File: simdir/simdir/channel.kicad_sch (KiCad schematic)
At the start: 80 parts, among them Q1 BC847, Q10 BC847, Q11 BC847, Q12 BC847, Q13 BC847, Q14 BC847, Q15 BC847, Q16 BC847, Q2 BC847, Q3 BC847, Q4 BC847, Q5 BC847, Q6 BC847, Q7 BC847, Q8 BC847, Q9 BC847, U1 MASWSS0178, U10 MASWSS0178, U11 MASWSS0178, U12 MASWSS0178, U13 MASWSS0178, U14 MASWSS0178, U15 MASWSS0178, U16 MASWSS0178, U17 LTV-847S, U18 LTV-847S, U19 74HCT595, U2 MASWSS0178, U3 MASWSS0178, U4 MASWSS0178, U5 MASWSS0178, U6 MASWSS0178, U7 MASWSS0178, U8 MASWSS0178, U9 MASWSS0178

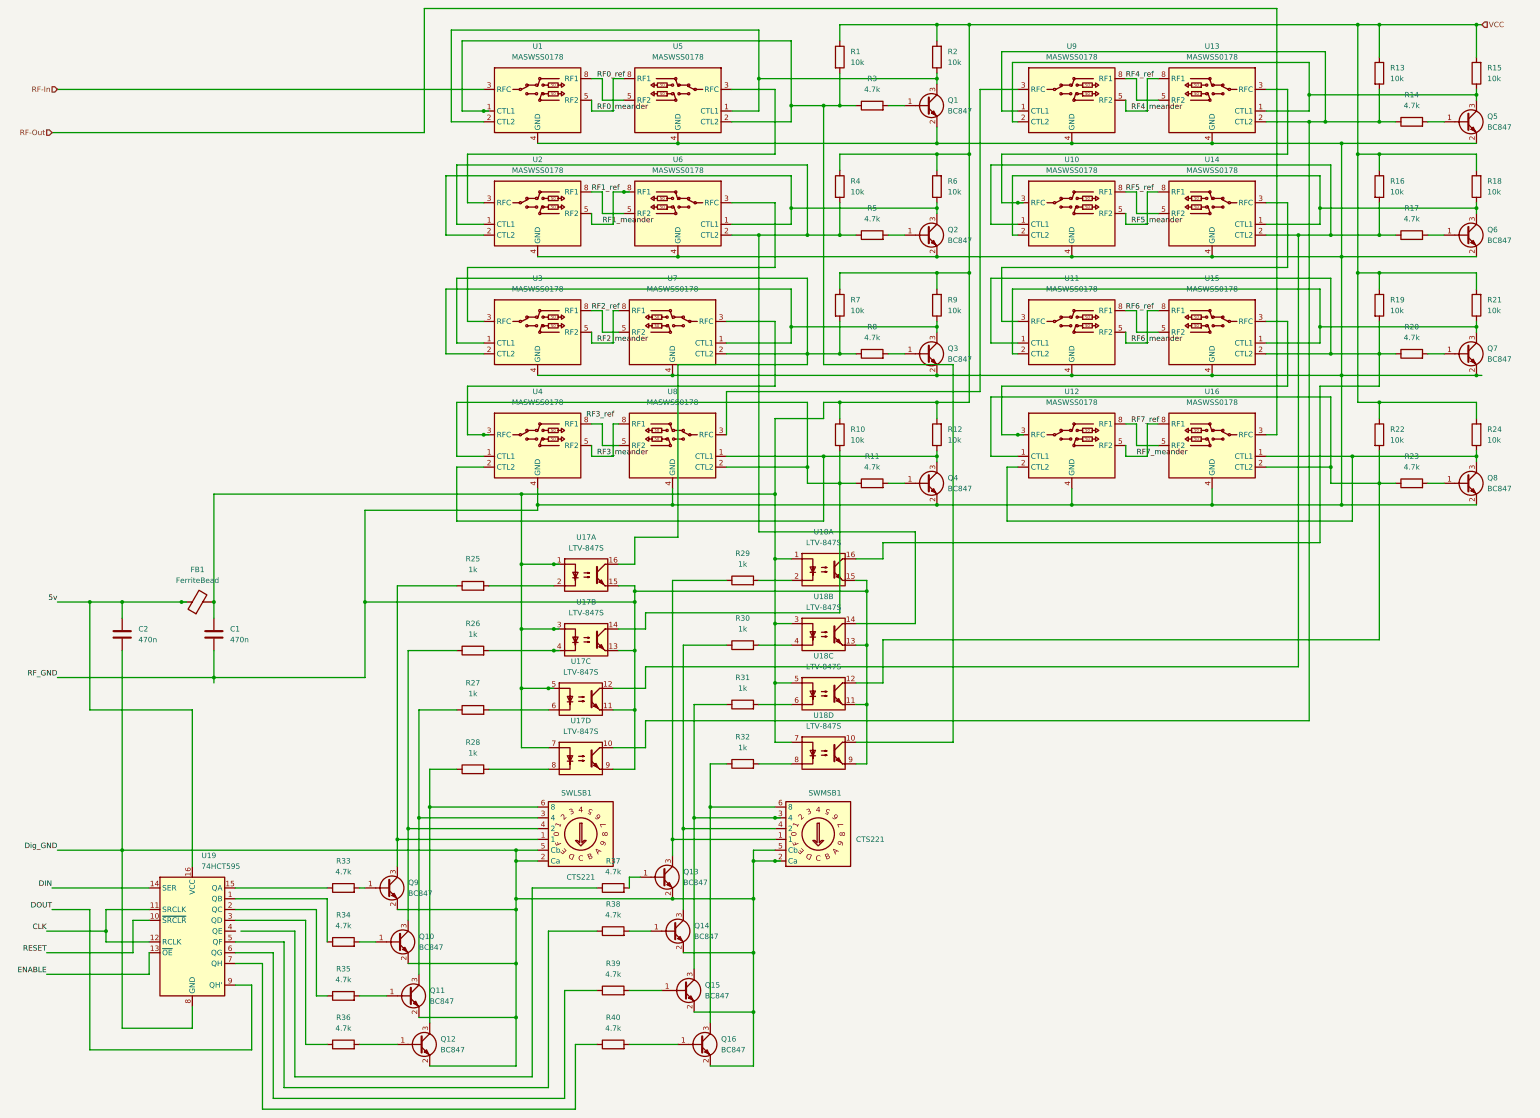
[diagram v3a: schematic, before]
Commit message: Finished channel layout.
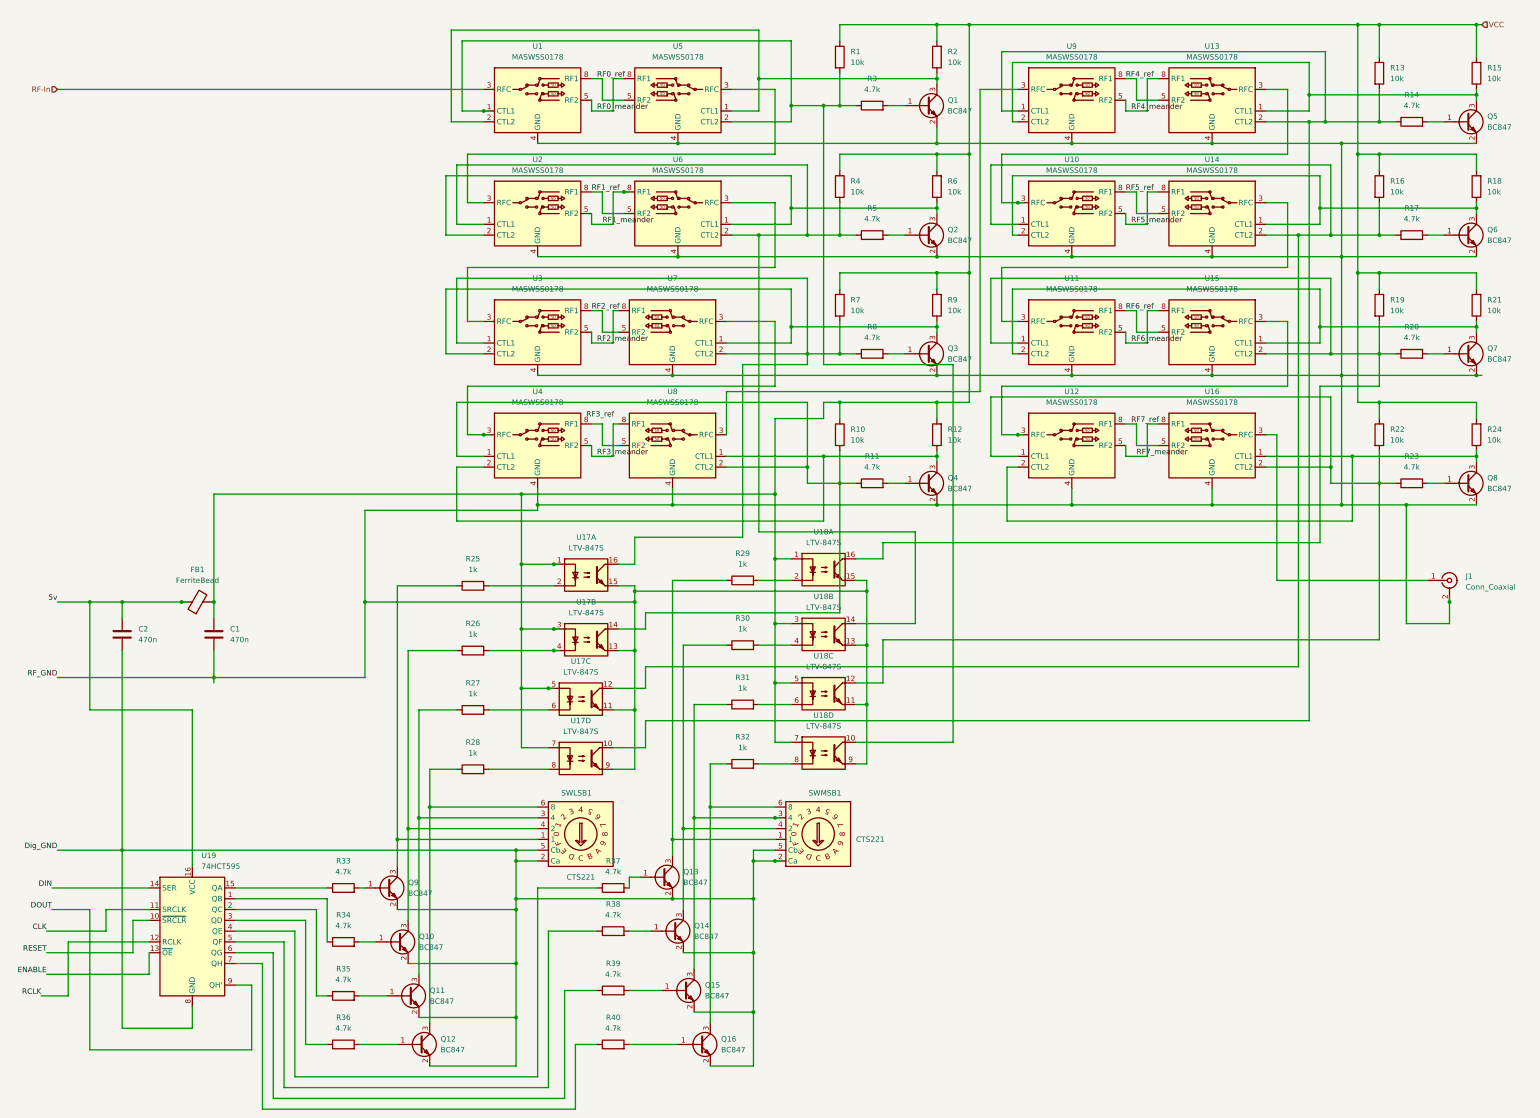
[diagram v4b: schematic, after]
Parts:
- added J1: Conn_Coaxial, Connector_Coaxial:SMA_Amphenol_132289_EdgeMount, symbol Connector:Conn_Coaxial
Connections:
- net CLK: no longer U19.12 (RCLK)
- net RF_GND: now also J1.2 (Ext)
- net at U19.4 (QE): now also R37.1
- net RF-Out: no longer names the net of U16.3 (RFC)
- net RF-Out: now also J1.1 (In)
- new net RCLK: U19.12 (RCLK)

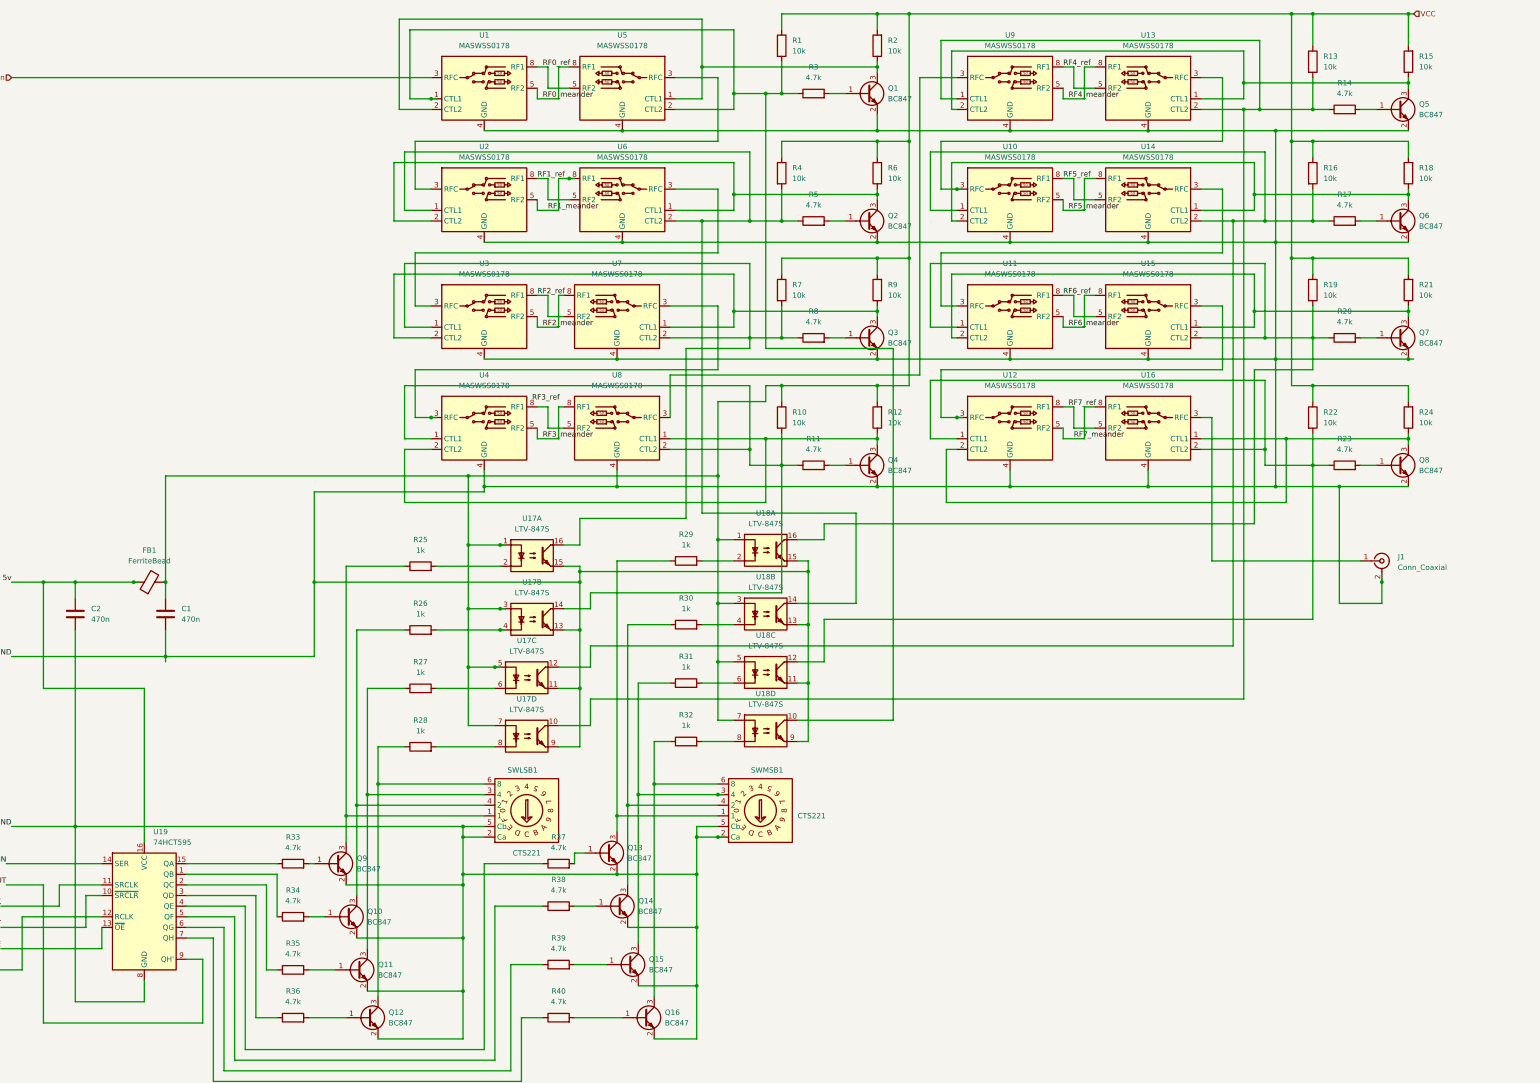
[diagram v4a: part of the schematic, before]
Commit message: Finalized channel design.
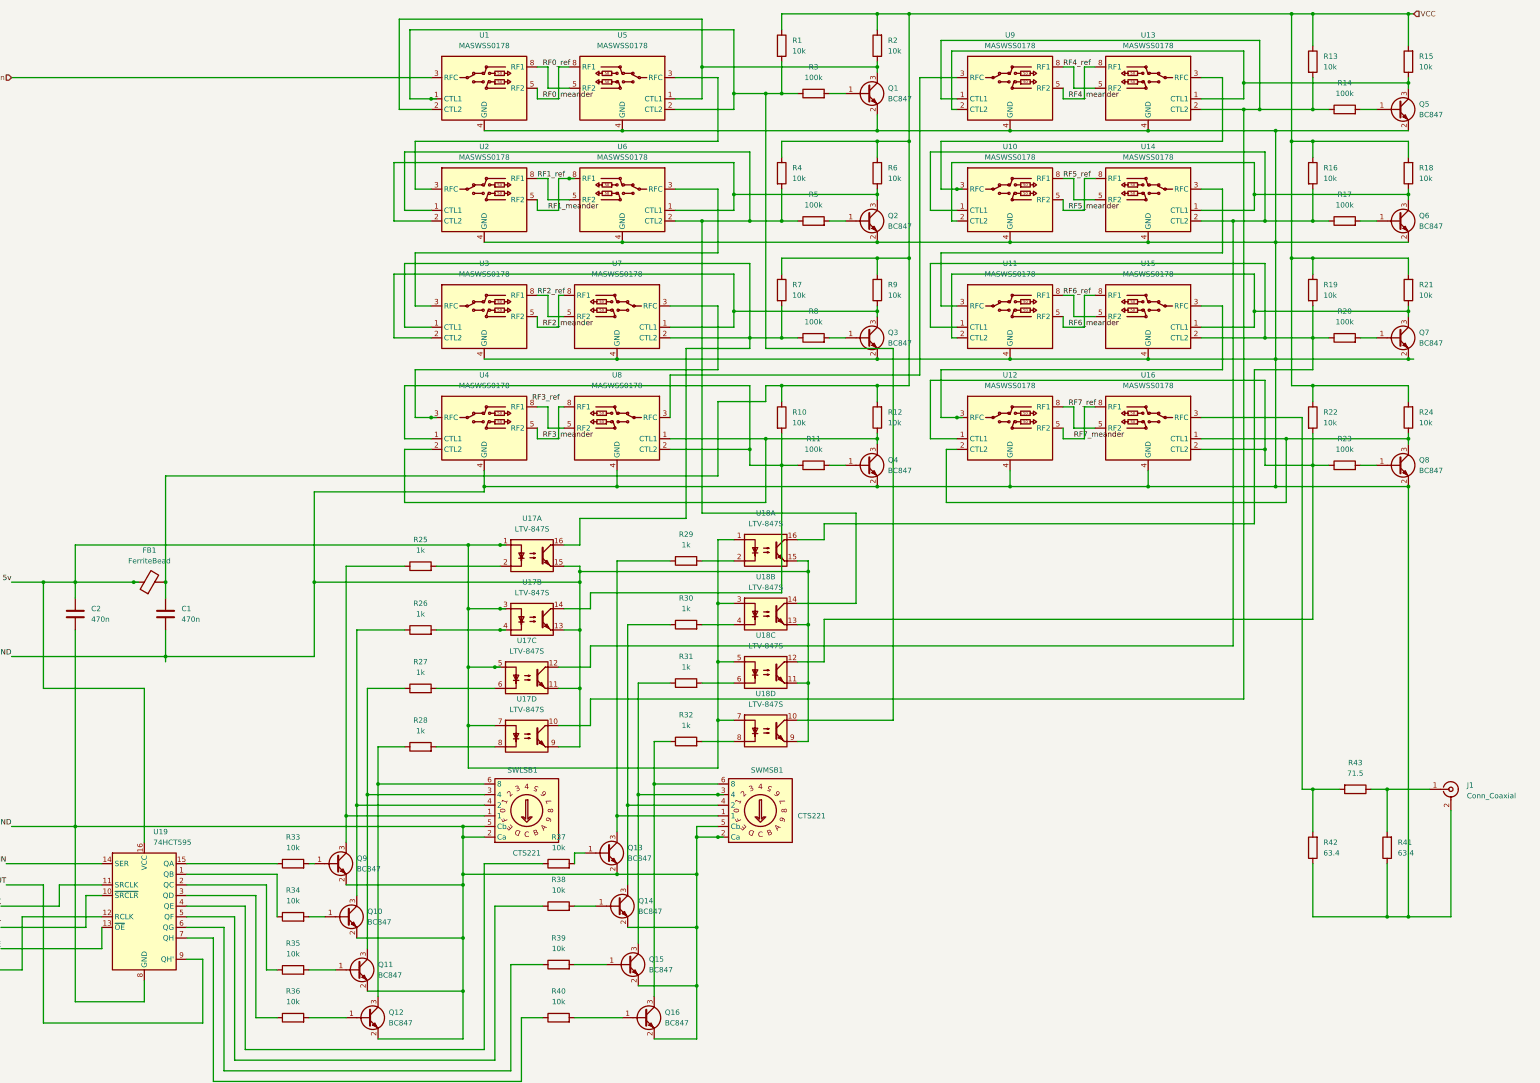
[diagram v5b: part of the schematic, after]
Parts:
- added R41, R42: 63.4, Resistor_SMD:R_0805_2012Metric_Pad1.20x1.40mm_HandSolder, symbol Device:R
- added R43: 71.5, Resistor_SMD:R_0805_2012Metric_Pad1.20x1.40mm_HandSolder, symbol Device:R
- R11, R14, R17, R20, R23, R3, R5, R8: value 4.7k -> 100k
- R33, R34, R35, R36, R37, R38, R39, R40: value 4.7k -> 10k
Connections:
- net 5v: now also U17.1, U17.3, U17.5, U17.7, U18.1, U18.3, U18.5, U18.7
- net RF_GND: now also R41.1, R42.1
- net VCC: no longer U17.1, U17.3, U17.5, U17.7, U18.1, U18.3, U18.5, U18.7
- net at U16.3 (RFC): now also R42.2, R43.2; no longer J1.1 (In)
- new net: J1.1 (In), R41.2, R43.1
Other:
- moved on the sheet: J1
